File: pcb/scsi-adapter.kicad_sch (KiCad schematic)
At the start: 0 parts

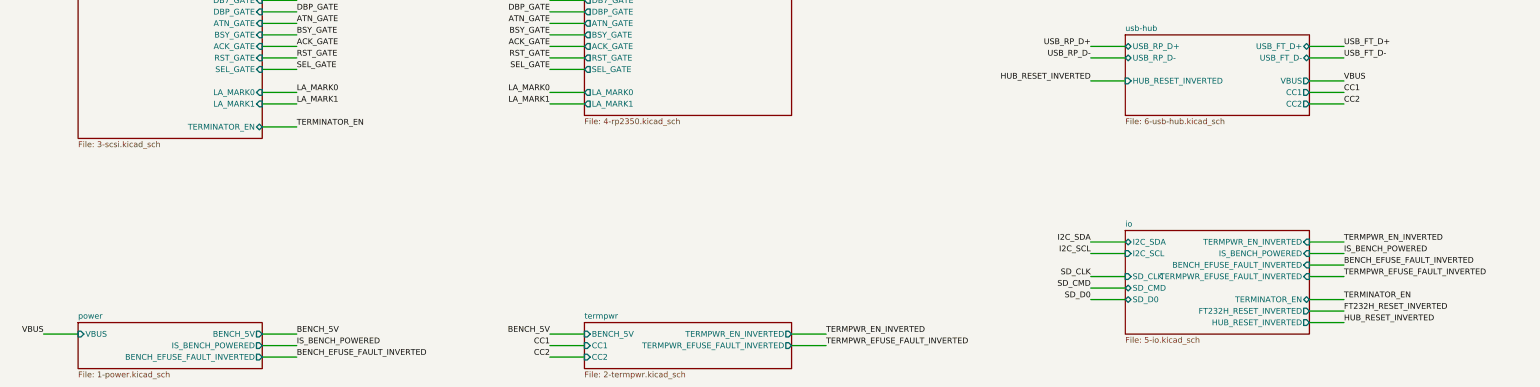
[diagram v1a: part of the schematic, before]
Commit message: Phase 3: populate SCSI sheet and channel sheets
SCSI sheet (A2): IDC50 and HD50 wired by signal name from SCSI-2
Table 2, all four RESERVED lines grounded through 0R links, the
logic-analyzer header as a pin-for-pin copy of the Digital Discovery
DIN connector, three SN74LVTH245A terminators with their DIP-switch
enable and truth table, and one cluster per line: 2 x 220R terminator
pair, ESD diode and channel sheet. Channel sheets hold the FDV301N
driver and the 74LVC1G17 receiver; 18 instances, references page x 100.

Generator: repeated sheets, sheet symbols, native tables, and
deterministic UUIDs. Nets renamed: LA -> LOGIC_ANALYZER,
TERMINATOR_EN -> TERMINATOR_EN_INVERTED_FIRMWARE.
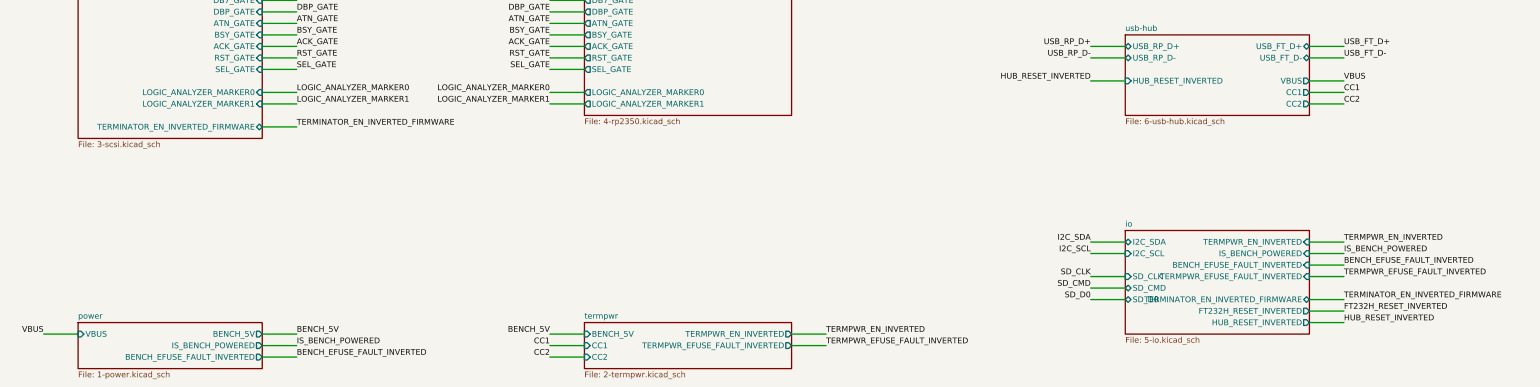
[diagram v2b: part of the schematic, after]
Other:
- sheet io ports: added TERMINATOR_EN_INVERTED_FIRMWARE; removed TERMINATOR_EN
- sheet rp2350 ports: added LOGIC_ANALYZER_MARKER0, LOGIC_ANALYZER_MARKER1; removed LA_MARK0, LA_MARK1
- sheet scsi ports: added LOGIC_ANALYZER_MARKER0, LOGIC_ANALYZER_MARKER1, TERMINATOR_EN_INVERTED_FIRMWARE; removed LA_MARK0, LA_MARK1, TERMINATOR_EN
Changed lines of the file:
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@@
 		)
 	)
-	(label "LA_MARK0"
+	(label "LOGIC_ANALYZER_MARKER0"
 		(at 144.78 114.3 180)
 		(effects
@@
 		)
 	)
-	(label "LA_MARK1"
+	(label "LOGIC_ANALYZER_MARKER1"
 		(at 144.78 116.84 180)
 		(effects
@@
 		)
 	)
-	(label "TERMINATOR_EN"
+	(label "TERMINATOR_EN_INVERTED_FIRMWARE"
 		(at 88.9 121.92 0)
 		(effects
@@
 		)
 	)
-	(label "LA_MARK0"
+	(label "LOGIC_ANALYZER_MARKER0"
 		(at 88.9 114.3 0)
 		(effects
@@
 		)
 	)
-	(label "LA_MARK1"
+	(label "LOGIC_ANALYZER_MARKER1"
 		(at 88.9 116.84 0)
 		(effects
@@
 		)
 	)
-	(label "TERMINATOR_EN"
+	(label "TERMINATOR_EN_INVERTED_FIRMWARE"
 		(at 320.04 160.02 0)
 		(effects
@@
 			)
 		)
-		(pin "LA_MARK0" output
+		(pin "LOGIC_ANALYZER_MARKER0" output
 			(at 152.4 114.3 180)
 			(effects
@@
 			)
 		)
-		(pin "LA_MARK1" output
+		(pin "LOGIC_ANALYZER_MARKER1" output
 			(at 152.4 116.84 180)
 			(effects
@@
 			)
 		)
-		(pin "LA_MARK0" input
+		(pin "LOGIC_ANALYZER_MARKER0" input
 			(at 81.28 114.3 0)
 			(effects
@@
 			)
 		)
-		(pin "LA_MARK1" input
+		(pin "LOGIC_ANALYZER_MARKER1" input
 			(at 81.28 116.84 0)
 			(effects
@@
 			)
 		)
-		(pin "TERMINATOR_EN" bidirectional
+		(pin "TERMINATOR_EN_INVERTED_FIRMWARE" bidirectional
 			(at 81.28 121.92 0)
 			(effects
@@
 			)
 		)
-		(pin "TERMINATOR_EN" bidirectional
+		(pin "TERMINATOR_EN_INVERTED_FIRMWARE" bidirectional
 			(at 312.42 160.02 0)
 			(effects

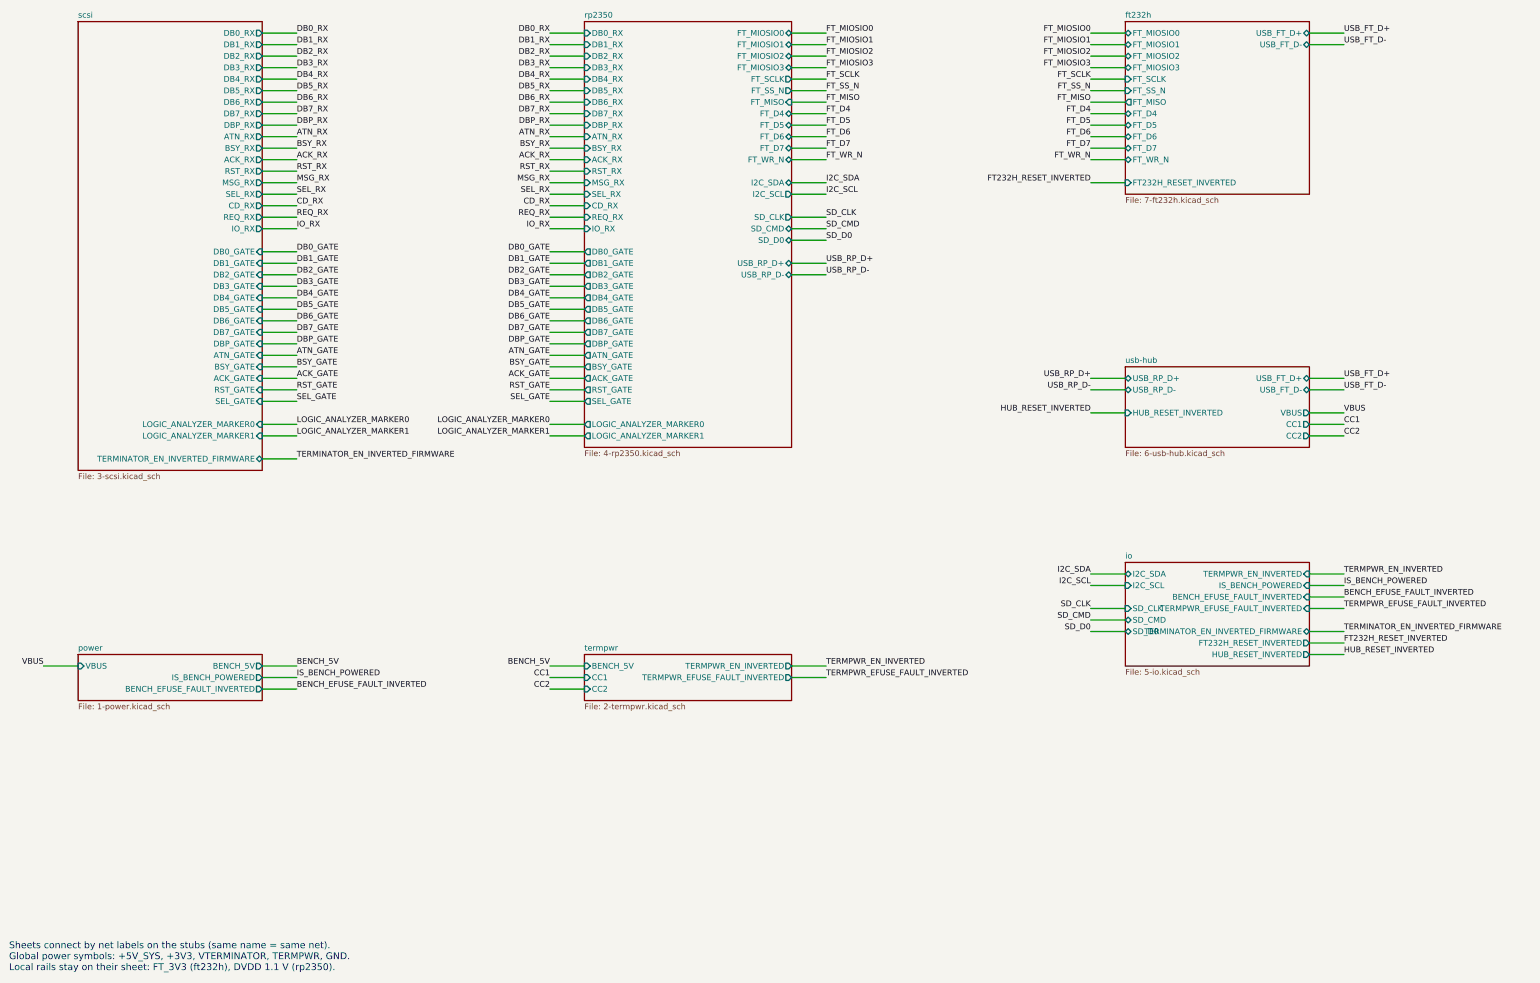
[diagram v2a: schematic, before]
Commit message: Phase 3: populate RP2350 sheet; FT_* nets renamed FT232H_*
RP2350 sheet (A2): RP2350B with every pin labelled by function and the
FT1248, marker and USB series resistors inline on their pins; core
regulator, per-pin decoupling (14 x 100 nF, count corrected), crystal,
QSPI flash and PSRAM in separate boxes, TC2030 debug pads and buttons,
the FT1248 rework links, and the TERMPWR sense divider on ADC6.

Generator: recursive derived-symbol flattening, small field fonts.
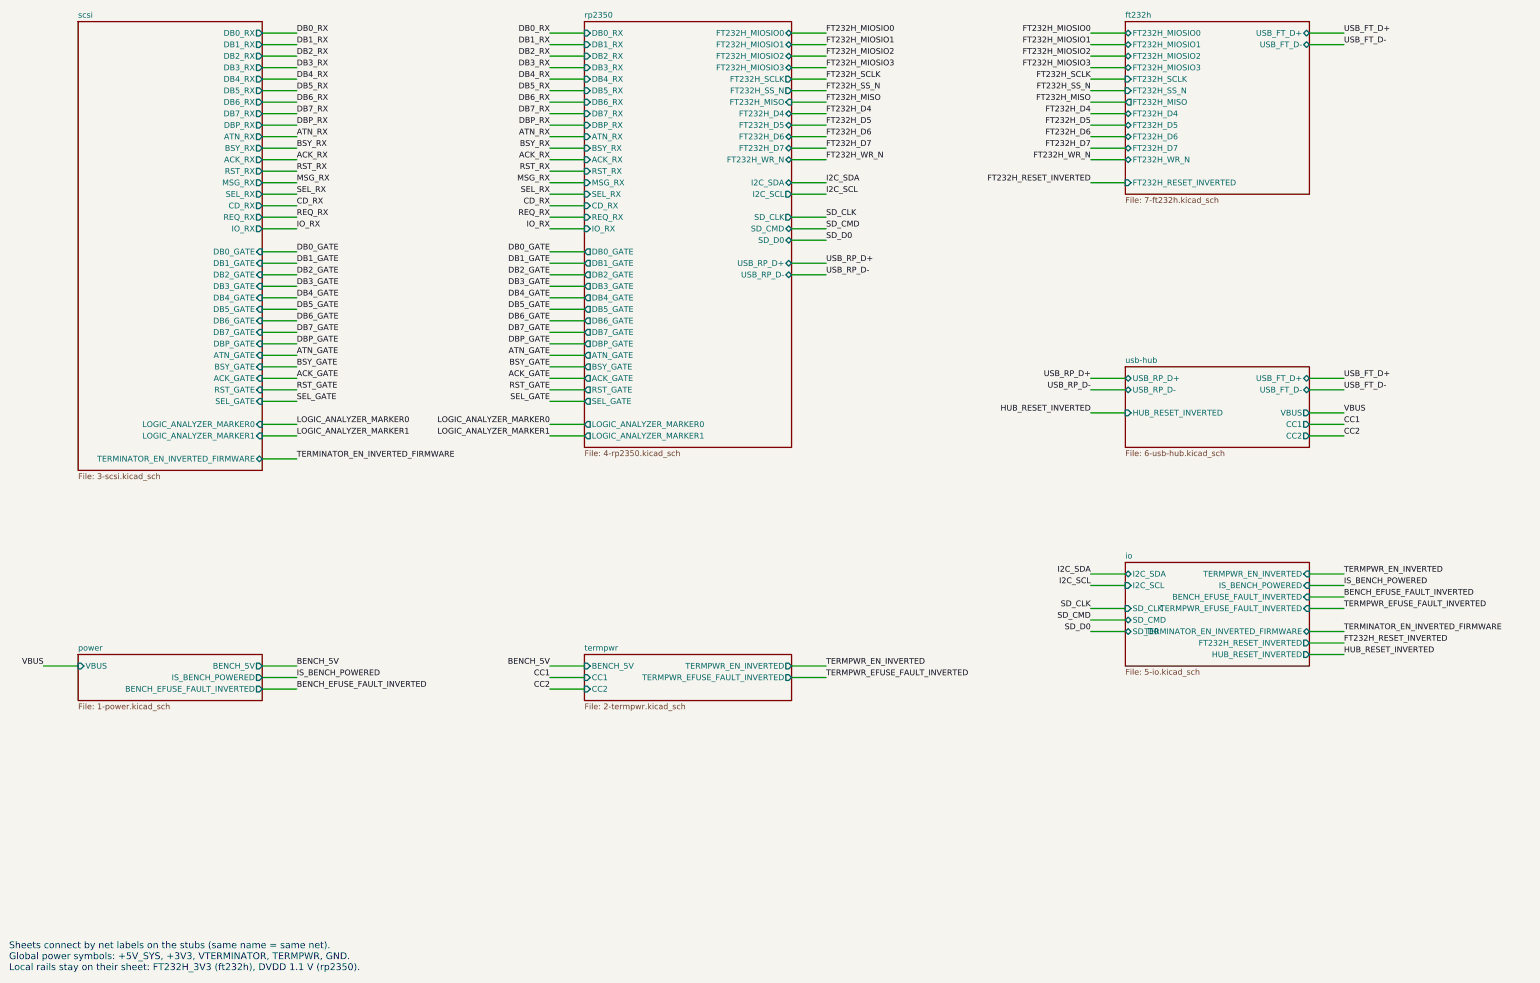
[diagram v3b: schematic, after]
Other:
- sheet ft232h ports: added FT232H_D4, FT232H_D5, FT232H_D6, FT232H_D7, FT232H_MIOSIO0, FT232H_MIOSIO1, FT232H_MIOSIO2, FT232H_MIOSIO3, FT232H_MISO, FT232H_SCLK, FT232H_SS_N, FT232H_WR_N; removed FT_D4, FT_D5, FT_D6, FT_D7, FT_MIOSIO0, FT_MIOSIO1, FT_MIOSIO2, FT_MIOSIO3, FT_MISO, FT_SCLK, FT_SS_N, FT_WR_N
- sheet rp2350 ports: added FT232H_D4, FT232H_D5, FT232H_D6, FT232H_D7, FT232H_MIOSIO0, FT232H_MIOSIO1, FT232H_MIOSIO2, FT232H_MIOSIO3, FT232H_MISO, FT232H_SCLK, FT232H_SS_N, FT232H_WR_N; removed FT_D4, FT_D5, FT_D6, FT_D7, FT_MIOSIO0, FT_MIOSIO1, FT_MIOSIO2, FT_MIOSIO3, FT_MISO, FT_SCLK, FT_SS_N, FT_WR_N
- note added: "Sheets connect by net labels on the stubs (same name = same net). Global power symbols: +5V_SYS, +3V3, VTERMINATOR, TERMPWR, GND. Local rails stay on their sheet: FT232H_3V3 (ft232h), DVDD 1.1 V (rp2350)."
- note removed: "Sheets connect by net labels on the stubs (same name = same net). Global power symbols: +5V_SYS, +3V3, VTERMINATOR, TERMPWR, GND. Local rails stay on their sheet: FT_3V3 (ft232h), DVDD 1.1 V (rp2350)."
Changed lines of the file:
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@@
 		(rev "0.1")
 	)
-	(text "Sheets connect by net labels on the stubs (same name = same net).\nGlobal power symbols: +5V_SYS, +3V3, VTERMINATOR, TERMPWR, GND.\nLocal rails stay on their sheet: FT_3V3 (ft232h), DVDD 1.1 V (rp2350)."
+	(text "Sheets connect by net labels on the stubs (same name = same net).\nGlobal power symbols: +5V_SYS, +3V3, VTERMINATOR, TERMPWR, GND.\nLocal rails stay on their sheet: FT232H_3V3 (ft232h), DVDD 1.1 V (rp2350)."
 		(exclude_from_sim no)
 		(at 25.4 228.6 0)
@@
 		)
 	)
-	(label "FT_MIOSIO3"
+	(label "FT232H_MIOSIO3"
 		(at 264.16 35.56 180)
 		(effects
@@
 		)
 	)
-	(label "FT_MISO"
+	(label "FT232H_MISO"
 		(at 264.16 43.18 180)
 		(effects
@@
 		)
 	)
-	(label "FT_MIOSIO0"
+	(label "FT232H_MIOSIO0"
 		(at 264.16 27.94 180)
 		(effects
@@
 		)
 	)
-	(label "FT_D7"
+	(label "FT232H_D7"
 		(at 205.74 53.34 0)
 		(effects
@@
 		)
 	)
-	(label "FT_SCLK"
+	(label "FT232H_SCLK"
 		(at 264.16 38.1 180)
 		(effects
@@
 		)
 	)
-	(label "FT_MIOSIO1"
+	(label "FT232H_MIOSIO1"
 		(at 264.16 30.48 180)
 		(effects
@@
 		)
 	)
-	(label "FT_WR_N"
+	(label "FT232H_WR_N"
 		(at 205.74 55.88 0)
 		(effects
@@
 		)
 	)
-	(label "FT_MIOSIO1"
+	(label "FT232H_MIOSIO1"
 		(at 205.74 30.48 0)
 		(effects
@@
 		)
 	)
-	(label "FT_D5"
+	(label "FT232H_D5"
 		(at 264.16 48.26 180)
 		(effects
@@
 		)
 	)
-	(label "FT_D5"
+	(label "FT232H_D5"
 		(at 205.74 48.26 0)
 		(effects
@@
 		)
 	)
-	(label "FT_SCLK"
+	(label "FT232H_SCLK"
 		(at 205.74 38.1 0)
 		(effects
@@
 		)
 	)
-	(label "FT_D4"
+	(label "FT232H_D4"
 		(at 205.74 45.72 0)
 		(effects
@@
 		)
 	)
-	(label "FT_D4"
+	(label "FT232H_D4"
 		(at 264.16 45.72 180)
 		(effects
@@
 		)
 	)
-	(label "FT_SS_N"
+	(label "FT232H_SS_N"
 		(at 264.16 40.64 180)
 		(effects
@@
 		)
 	)
-	(label "FT_MIOSIO3"
+	(label "FT232H_MIOSIO3"
 		(at 205.74 35.56 0)
 		(effects
@@
 		)
 	)
-	(label "FT_D6"
+	(label "FT232H_D6"
 		(at 264.16 50.8 180)
 		(effects
@@
 		)
 	)
-	(label "FT_MIOSIO0"
+	(label "FT232H_MIOSIO0"
 		(at 205.74 27.94 0)
 		(effects
@@
 		)
 	)
-	(label "FT_D6"
+	(label "FT232H_D6"
 		(at 205.74 50.8 0)
 		(effects
@@
 		)
 	)
-	(label "FT_WR_N"
+	(label "FT232H_WR_N"
 		(at 264.16 55.88 180)
 		(effects
@@
 		)
 	)
-	(label "FT_MIOSIO2"
+	(label "FT232H_MIOSIO2"
 		(at 205.74 33.02 0)
 		(effects
@@
 		)
 	)
-	(label "FT_SS_N"
+	(label "FT232H_SS_N"
 		(at 205.74 40.64 0)
 		(effects
@@
 		)
 	)
-	(label "FT_MISO"
+	(label "FT232H_MISO"
 		(at 205.74 43.18 0)
 		(effects
@@
 		)
 	)
-	(label "FT_MIOSIO2"
+	(label "FT232H_MIOSIO2"
 		(at 264.16 33.02 180)
 		(effects
@@
 		)
 	)
-	(label "FT_D7"
+	(label "FT232H_D7"
 		(at 264.16 53.34 180)
 		(effects
@@
 			)
 		)
-		(pin "FT_MIOSIO0" bidirectional
+		(pin "FT232H_MIOSIO0" bidirectional
 			(at 198.12 27.94 0)
 			(effects
@@
 			)
 		)
-		(pin "FT_MIOSIO1" bidirectional
+		(pin "FT232H_MIOSIO1" bidirectional
 			(at 198.12 30.48 0)
 			(effects
@@
 			)
 		)
-		(pin "FT_MIOSIO2" bidirectional
+		(pin "FT232H_MIOSIO2" bidirectional
 			(at 198.12 33.02 0)
 			(effects
@@
 			)
 		)
-		(pin "FT_MIOSIO3" bidirectional
+		(pin "FT232H_MIOSIO3" bidirectional
 			(at 198.12 35.56 0)
 			(effects
@@
 			)
 		)
-		(pin "FT_SCLK" output
+		(pin "FT232H_SCLK" output
 			(at 198.12 38.1 0)
 			(effects
@@
 			)
 		)
-		(pin "FT_SS_N" output
+		(pin "FT232H_SS_N" output
 			(at 198.12 40.64 0)
 			(effects
@@
 			)
 		)
-		(pin "FT_MISO" input
+		(pin "FT232H_MISO" input
 			(at 198.12 43.18 0)
 			(effects
@@
 			)
 		)
-		(pin "FT_D4" bidirectional
+		(pin "FT232H_D4" bidirectional
 			(at 198.12 45.72 0)
 			(effects
@@
 			)
 		)
-		(pin "FT_D5" bidirectional
+		(pin "FT232H_D5" bidirectional
 			(at 198.12 48.26 0)
 			(effects
@@
 			)
 		)
-		(pin "FT_D6" bidirectional
+		(pin "FT232H_D6" bidirectional
 			(at 198.12 50.8 0)
 			(effects
@@
 			)
 		)
-		(pin "FT_D7" bidirectional
+		(pin "FT232H_D7" bidirectional
 			(at 198.12 53.34 0)
 			(effects
@@
 			)
 		)
-		(pin "FT_WR_N" bidirectional
+		(pin "FT232H_WR_N" bidirectional
 			(at 198.12 55.88 0)
 			(effects
@@
 			)
 		)
-		(pin "FT_MIOSIO0" bidirectional
+		(pin "FT232H_MIOSIO0" bidirectional
 			(at 271.78 27.94 180)
 			(effects
@@
 			)
 		)
-		(pin "FT_MIOSIO1" bidirectional
+		(pin "FT232H_MIOSIO1" bidirectional
 			(at 271.78 30.48 180)
 			(effects
@@
 			)
 		)
-		(pin "FT_MIOSIO2" bidirectional
+		(pin "FT232H_MIOSIO2" bidirectional
 			(at 271.78 33.02 180)
 			(effects
@@
 			)
 		)
-		(pin "FT_MIOSIO3" bidirectional
+		(pin "FT232H_MIOSIO3" bidirectional
 			(at 271.78 35.56 180)
 			(effects
@@
 			)
 		)
-		(pin "FT_SCLK" input
+		(pin "FT232H_SCLK" input
 			(at 271.78 38.1 180)
 			(effects
@@
 			)
 		)
-		(pin "FT_SS_N" input
+		(pin "FT232H_SS_N" input
 			(at 271.78 40.64 180)
 			(effects
@@
 			)
 		)
-		(pin "FT_MISO" output
+		(pin "FT232H_MISO" output
 			(at 271.78 43.18 180)
 			(effects
@@
 			)
 		)
-		(pin "FT_D4" bidirectional
+		(pin "FT232H_D4" bidirectional
 			(at 271.78 45.72 180)
 			(effects
@@
 			)
 		)
-		(pin "FT_D5" bidirectional
+		(pin "FT232H_D5" bidirectional
 			(at 271.78 48.26 180)
 			(effects
@@
 			)
 		)
-		(pin "FT_D6" bidirectional
+		(pin "FT232H_D6" bidirectional
 			(at 271.78 50.8 180)
 			(effects
@@
 			)
 		)
-		(pin "FT_D7" bidirectional
+		(pin "FT232H_D7" bidirectional
 			(at 271.78 53.34 180)
 			(effects
@@
 			)
 		)
-		(pin "FT_WR_N" bidirectional
+		(pin "FT232H_WR_N" bidirectional
 			(at 271.78 55.88 180)
 			(effects

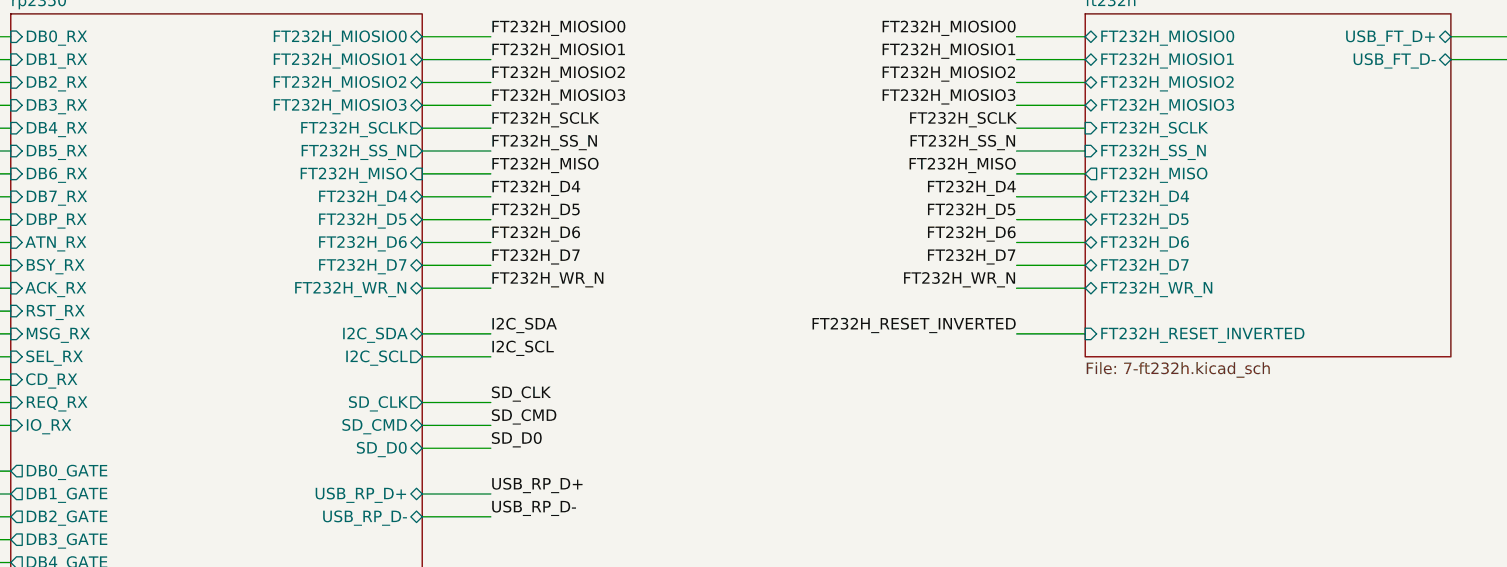
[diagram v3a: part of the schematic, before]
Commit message: Phase 3: populate FT232H sheet; FT232H_WR_N -> FT232H_WRITE_INVERTED
FT232HL per DS Fig. 6.2 (VCCD makes FT232H_3V3), ferrite-fed VPHY/VPLL,
93LC56B config EEPROM, crystal, REF, RESET RC and FIFO-fallback pull-ups.
Project FT232H symbol retypes EECS/EECLK as outputs (and VCCD as
power_out); upstream fix recorded as a follow-up (NOTES open question 14).
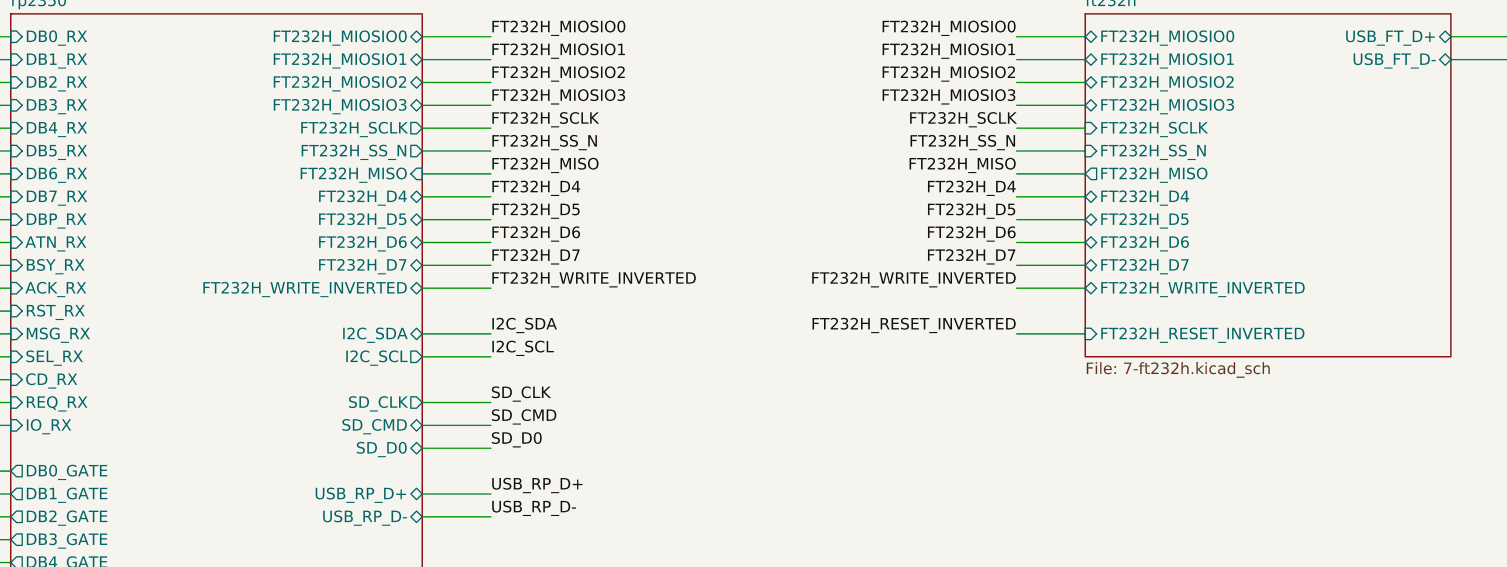
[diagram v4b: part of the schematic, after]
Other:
- sheet ft232h ports: added FT232H_WRITE_INVERTED; removed FT232H_WR_N
- sheet rp2350 ports: added FT232H_WRITE_INVERTED; removed FT232H_WR_N
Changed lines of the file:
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@@
 		)
 	)
-	(label "FT232H_WR_N"
+	(label "FT232H_WRITE_INVERTED"
 		(at 205.74 55.88 0)
 		(effects
@@
 		)
 	)
-	(label "FT232H_WR_N"
+	(label "FT232H_WRITE_INVERTED"
 		(at 264.16 55.88 180)
 		(effects
@@
 			)
 		)
-		(pin "FT232H_WR_N" bidirectional
+		(pin "FT232H_WRITE_INVERTED" bidirectional
 			(at 198.12 55.88 0)
 			(effects
@@
 			)
 		)
-		(pin "FT232H_WR_N" bidirectional
+		(pin "FT232H_WRITE_INVERTED" bidirectional
 			(at 271.78 55.88 180)
 			(effects
